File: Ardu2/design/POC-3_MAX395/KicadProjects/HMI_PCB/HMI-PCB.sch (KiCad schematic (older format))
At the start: 37 parts, among them P1 SplitPot_0_M, P10 TREM_VIB, P11 SplitPot_5_TR, P12 Analog Power IN, P13 Digital Power IN/OUT, P2 SEQ_SAVE, P3 SplitPot_1_A, P4 SplitPot_2_B, P5 PB_OUT, P6 Analog_Out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

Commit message: updated peripherals PCB
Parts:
- C1, C2, C3, C4, C5, C6: footprint Capacitors_ThroughHole:C_Radial_D5_L11_P2 -> misc:C_Radial_D5_L11_P3.81
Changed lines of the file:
@@
 F 0 "C1" H 1877 6935 50  0000 L CNN
 F 1 "1µF" H 1877 6846 50  0000 L CNN
-F 2 "Capacitors_ThroughHole:C_Radial_D5_L11_P2" H 1798 6740 50  0001 C CNN
+F 2 "misc:C_Radial_D5_L11_P3.81" H 1798 6740 50  0001 C CNN
 F 3 "" H 1760 6890 50  0000 C CNN
 	1    1760 6890
@@
 F 0 "C2" H 2527 6935 50  0000 L CNN
 F 1 "1µF" H 2527 6846 50  0000 L CNN
-F 2 "Capacitors_ThroughHole:C_Radial_D5_L11_P2" H 2448 6740 50  0001 C CNN
+F 2 "misc:C_Radial_D5_L11_P3.81" H 2448 6740 50  0001 C CNN
 F 3 "" H 2410 6890 50  0000 C CNN
 	1    2410 6890
@@
 F 0 "C5" H 4477 6935 50  0000 L CNN
 F 1 "1µF" H 4477 6846 50  0000 L CNN
-F 2 "Capacitors_ThroughHole:C_Radial_D5_L11_P2" H 4398 6740 50  0001 C CNN
+F 2 "misc:C_Radial_D5_L11_P3.81" H 4398 6740 50  0001 C CNN
 F 3 "" H 4360 6890 50  0000 C CNN
 	1    4360 6890
@@
 F 0 "C6" H 5127 6935 50  0000 L CNN
 F 1 "1µF" H 5127 6846 50  0000 L CNN
-F 2 "Capacitors_ThroughHole:C_Radial_D5_L11_P2" H 5048 6740 50  0001 C CNN
+F 2 "misc:C_Radial_D5_L11_P3.81" H 5048 6740 50  0001 C CNN
 F 3 "" H 5010 6890 50  0000 C CNN
 	1    5010 6890
@@
 F 0 "C3" H 3177 6935 50  0000 L CNN
 F 1 "1µF" H 3177 6846 50  0000 L CNN
-F 2 "Capacitors_ThroughHole:C_Radial_D5_L11_P2" H 3098 6740 50  0001 C CNN
+F 2 "misc:C_Radial_D5_L11_P3.81" H 3098 6740 50  0001 C CNN
 F 3 "" H 3060 6890 50  0000 C CNN
 	1    3060 6890
@@
 F 0 "C4" H 3827 6935 50  0000 L CNN
 F 1 "1µF" H 3827 6846 50  0000 L CNN
-F 2 "Capacitors_ThroughHole:C_Radial_D5_L11_P2" H 3748 6740 50  0001 C CNN
+F 2 "misc:C_Radial_D5_L11_P3.81" H 3748 6740 50  0001 C CNN
 F 3 "" H 3710 6890 50  0000 C CNN
 	1    3710 6890

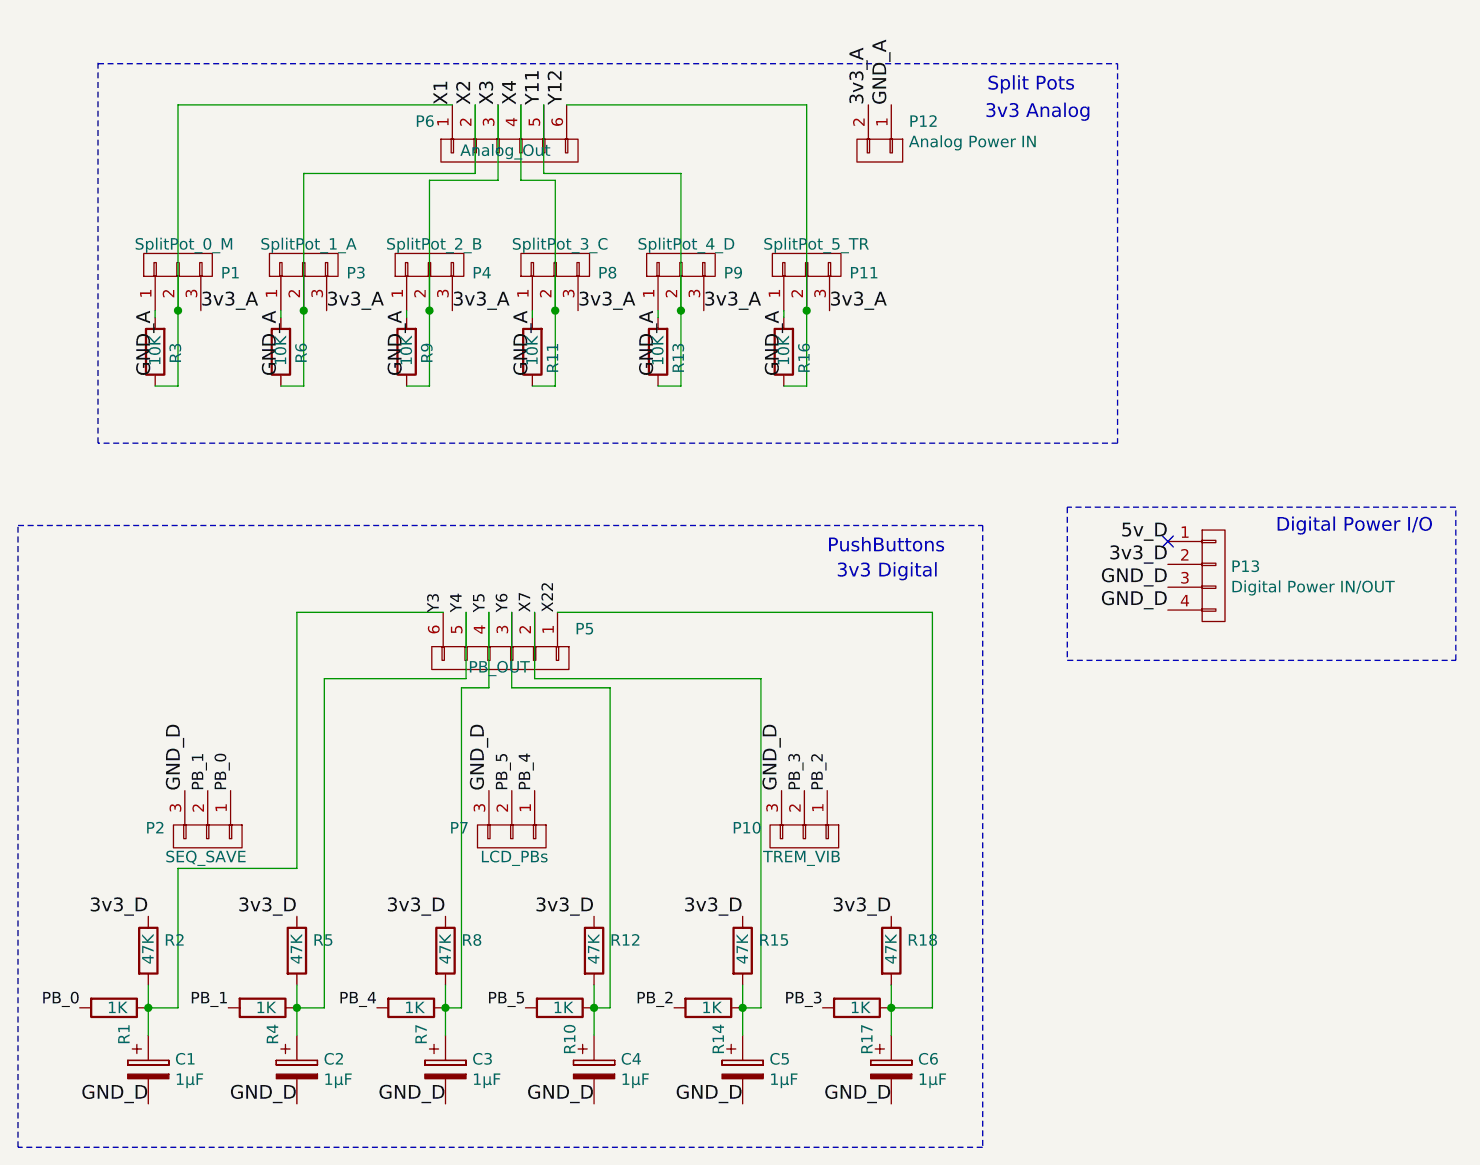
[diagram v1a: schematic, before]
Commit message: updated to HMI PCB after SENSEI review
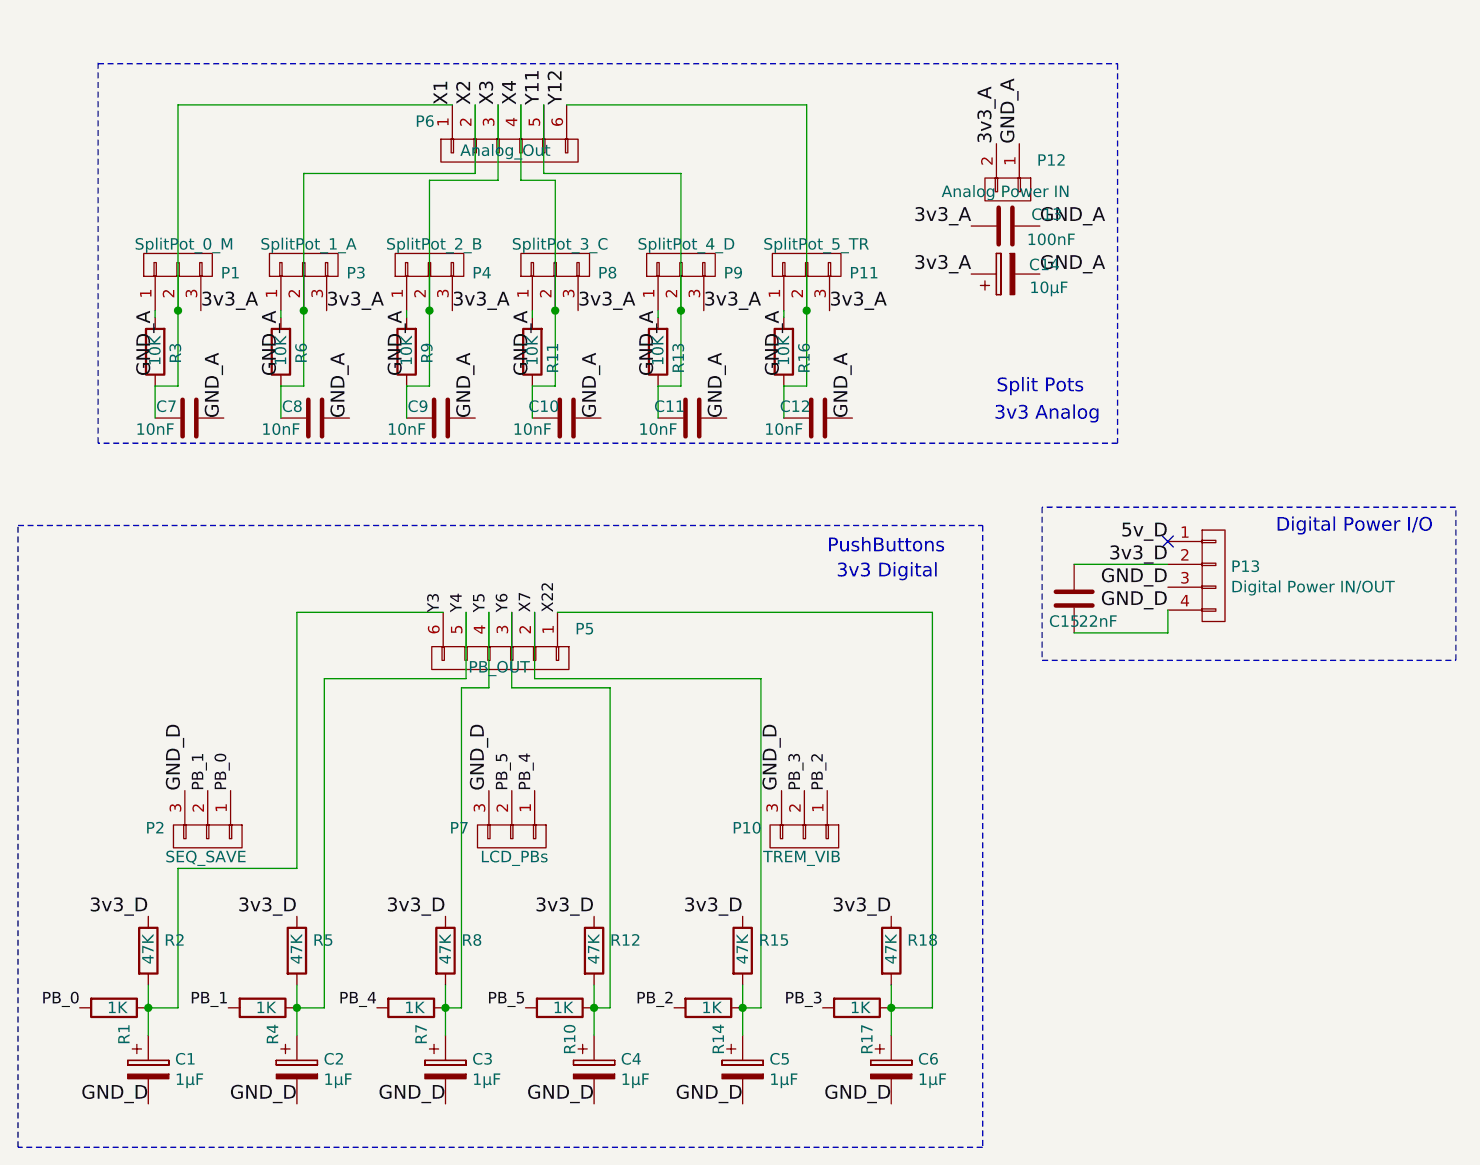
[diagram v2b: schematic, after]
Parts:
- added C10, C11, C12, C7, C8, C9: 10nF, Capacitors_ThroughHole:C_Disc_D6_P5, symbol C
- added C13: 100nF, Capacitors_ThroughHole:C_Disc_D3_P2.5, symbol C
- added C14: 10µF, Capacitors_ThroughHole:C_Radial_D5_L11_P2.5, symbol CP
- added C15: 22nF, Capacitors_ThroughHole:C_Rect_L7_W2.5_P5, symbol C
- P1, P10, P11, P2, P3, P4, P7, P8, P9: footprint Connect:Wafer_Horizontal10x5.8x7RM2.5-3 -> misc:Wafer_Angled_1x03_1mm_hole
- P12: footprint Pin_Headers:Pin_Header_Angled_1x02 -> misc:Wafer_Angled_1x02_1mm_hole
- P13: footprint Connect:bornier4 -> misc:bornier4_Dinkle
- P5, P6: footprint Connect:Wafer_Horizontal17.5x5.8x7RM2.5-6 -> misc:Wafer_Angled_1x06_1mm_Hole
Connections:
- net 3v3_A: now also C13.2, C14.1
- net 3v3_D: now also C15.1
- net GND_A: now also C10.1, C11.1, C12.1, C13.1, C14.2, C7.1, C8.1, C9.1
- net GND_D: now also C15.2
- net X1: now also C7.2
- net X2: now also C8.2
- net X3: now also C9.2
- net X4: now also C10.2
- net Y11: now also C11.2
- net Y12: now also C12.2
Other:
- moved on the sheet: P12
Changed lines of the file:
@@
 F 0 "P2" V 1984 5683 50  0000 R CNN
 F 1 "SEQ_SAVE" V 2110 6040 50  0000 R CNN
-F 2 "Connect:Wafer_Horizontal10x5.8x7RM2.5-3" H 2020 5870 50  0001 C CNN
+F 2 "misc:Wafer_Angled_1x03_1mm_hole" H 2020 5870 50  0001 C CNN
 F 3 "" H 2020 5870 50  0000 C CNN
 	1    2020 5870
@@
 F 0 "P1" V 1854 3183 50  0000 R CNN
 F 1 "SplitPot_0_M" V 1980 3560 50  0000 R CNN
-F 2 "Connect:Wafer_Horizontal10x5.8x7RM2.5-3" H 1890 3370 50  0001 C CNN
+F 2 "misc:Wafer_Angled_1x03_1mm_hole" H 1890 3370 50  0001 C CNN
 F 3 "" H 1890 3370 50  0000 C CNN
 	1    1890 3370
@@
 L CONN_01X02 P12
 U 1 1 580A7415
-P 4960 2870
-F 0 "P12" V 4833 2997 50  0000 L CNN
-F 1 "Analog Power IN" V 4922 2997 50  0000 L CNN
-F 2 "Pin_Headers:Pin_Header_Angled_1x02" H 4960 2870 50  0001 C CNN
-F 3 "" H 4960 2870 50  0000 C CNN
-	1    4960 2870
+P 5520 3040
+F 0 "P12" V 5393 3167 50  0000 L CNN
+F 1 "Analog Power IN" V 5530 2750 50  0000 L CNN
+F 2 "misc:Wafer_Angled_1x02_1mm_hole" H 5520 3040 50  0001 C CNN
+F 3 "" H 5520 3040 50  0000 C CNN
+	1    5520 3040
 	0    1    1    0
 $EndComp
@@
 F 0 "P6" V 3213 3197 50  0000 L CNN
 F 1 "Analog_Out" V 3340 2690 50  0000 L CNN
-F 2 "Connect:Wafer_Horizontal17.5x5.8x7RM2.5-6" H 3340 2870 50  0001 C CNN
+F 2 "misc:Wafer_Angled_1x06_1mm_Hole" H 3340 2870 50  0001 C CNN
 F 3 "" H 3340 2870 50  0000 C CNN
 	1    3340 2870
 	0    -1   1    0
 $EndComp
-Text Notes 5430 2620 0    60   ~ 0
+Text Notes 5470 3940 0    60   ~ 0
 Split Pots
 $Comp
@@
 F 0 "P5" V 3173 5417 50  0000 L CNN
 F 1 "PB_OUT" V 3340 4950 50  0000 L CNN
-F 2 "Connect:Wafer_Horizontal17.5x5.8x7RM2.5-6" H 3300 5090 50  0001 C CNN
+F 2 "misc:Wafer_Angled_1x06_1mm_Hole" H 3300 5090 50  0001 C CNN
 F 3 "" H 3300 5090 50  0000 C CNN
 	1    3300 5090
@@
 Text Notes 4770 4750 0    60   ~ 0
 3v3 Digital
-Text Notes 5420 2740 0    60   ~ 0
+Text Notes 5460 4060 0    60   ~ 0
 3v3 Analog
 $Comp
@@
 	1    0    0    -1
 $EndComp
-Text Label 4910 2670 1    60   ~ 0
+Text Label 5470 2840 1    60   ~ 0
 3v3_A
-Text Label 5010 2670 1    60   ~ 0
+Text Label 5570 2840 1    60   ~ 0
 GND_A
 Text Label 1790 3570 3    60   ~ 0
@@
 F 0 "P3" V 2404 3183 50  0000 R CNN
 F 1 "SplitPot_1_A" V 2530 3560 50  0000 R CNN
-F 2 "Connect:Wafer_Horizontal10x5.8x7RM2.5-3" H 2440 3370 50  0001 C CNN
+F 2 "misc:Wafer_Angled_1x03_1mm_hole" H 2440 3370 50  0001 C CNN
 F 3 "" H 2440 3370 50  0000 C CNN
 	1    2440 3370
@@
 F 0 "P4" V 2954 3183 50  0000 R CNN
 F 1 "SplitPot_2_B" V 3080 3560 50  0000 R CNN
-F 2 "Connect:Wafer_Horizontal10x5.8x7RM2.5-3" H 2990 3370 50  0001 C CNN
+F 2 "misc:Wafer_Angled_1x03_1mm_hole" H 2990 3370 50  0001 C CNN
 F 3 "" H 2990 3370 50  0000 C CNN
 	1    2990 3370
@@
 F 0 "P8" V 3504 3183 50  0000 R CNN
 F 1 "SplitPot_3_C" V 3630 3560 50  0000 R CNN
-F 2 "Connect:Wafer_Horizontal10x5.8x7RM2.5-3" H 3540 3370 50  0001 C CNN
+F 2 "misc:Wafer_Angled_1x03_1mm_hole" H 3540 3370 50  0001 C CNN
 F 3 "" H 3540 3370 50  0000 C CNN
 	1    3540 3370
@@
 F 0 "P9" V 4054 3183 50  0000 R CNN
 F 1 "SplitPot_4_D" V 4180 3560 50  0000 R CNN
-F 2 "Connect:Wafer_Horizontal10x5.8x7RM2.5-3" H 4090 3370 50  0001 C CNN
+F 2 "misc:Wafer_Angled_1x03_1mm_hole" H 4090 3370 50  0001 C CNN
 F 3 "" H 4090 3370 50  0000 C CNN
 	1    4090 3370
@@
 F 0 "P11" V 4604 3183 50  0000 R CNN
 F 1 "SplitPot_5_TR" V 4730 3560 50  0000 R CNN
-F 2 "Connect:Wafer_Horizontal10x5.8x7RM2.5-3" H 4640 3370 50  0001 C CNN
+F 2 "misc:Wafer_Angled_1x03_1mm_hole" H 4640 3370 50  0001 C CNN
 F 3 "" H 4640 3370 50  0000 C CNN
 	1    4640 3370
@@
 F 0 "P10" V 4594 5683 50  0000 R CNN
 F 1 "TREM_VIB" V 4720 6030 50  0000 R CNN
-F 2 "Connect:Wafer_Horizontal10x5.8x7RM2.5-3" H 4630 5870 50  0001 C CNN
+F 2 "misc:Wafer_Angled_1x03_1mm_hole" H 4630 5870 50  0001 C CNN
 F 3 "" H 4630 5870 50  0000 C CNN
 	1    4630 5870
@@
 F 0 "P7" V 3314 5683 50  0000 R CNN
 F 1 "LCD_PBs" V 3440 6030 50  0000 R CNN
-F 2 "Connect:Wafer_Horizontal10x5.8x7RM2.5-3" H 3350 5870 50  0001 C CNN
+F 2 "misc:Wafer_Angled_1x03_1mm_hole" H 3350 5870 50  0001 C CNN
 F 3 "" H 3350 5870 50  0000 C CNN
 	1    3350 5870
@@
 F 0 "P13" H 6496 4770 50  0000 L CNN
 F 1 "Digital Power IN/OUT" H 6496 4681 50  0000 L CNN
-F 2 "Connect:bornier4" H 6420 4730 50  0001 C CNN
+F 2 "misc:bornier4_Dinkle" H 6420 4730 50  0001 C CNN
 F 3 "" H 6420 4730 50  0000 C CNN
 	1    6420 4730
@@
 GND_D
 Wire Notes Line
-	5780 4430 5780 5100
-Wire Notes Line
-	5780 5100 7480 5100
+	5670 4430 5670 5100
+Wire Notes Line
+	5670 5100 7480 5100
 Wire Notes Line
 	7480 5100 7480 4430
 Wire Notes Line
-	7480 4430 5780 4430
+	7480 4430 5670 4430
 Text Notes 7380 4550 2    60   ~ 0
 Digital Power I/O
@@
 Connection ~ 4090 3570
 Connection ~ 4640 3570
+$Comp
+L C C13
+U 1 1 581098BB
+P 5510 3200
+F 0 "C13" V 5460 3380 50  0000 C CNN
+F 1 "100nF" V 5570 3400 50  0000 C CNN
+F 2 "Capacitors_ThroughHole:C_Disc_D3_P2.5" H 5548 3050 50  0001 C CNN
+F 3 "" H 5510 3200 50  0000 C CNN
+	1    5510 3200
+	0    1    1    0
+$EndComp
+$Comp
+L CP C14
+U 1 1 58109AF8
+P 5510 3410
+F 0 "C14" V 5550 3240 50  0000 C CNN
+F 1 "10µF" V 5450 3220 50  0000 C CNN
+F 2 "Capacitors_ThroughHole:C_Radial_D5_L11_P2.5" H 5548 3260 50  0001 C CNN
+F 3 "" H 5510 3410 50  0000 C CNN
+	1    5510 3410
+	0    -1   -1   0
+$EndComp
+Text Label 5360 3200 2    60   ~ 0
+3v3_A
+Text Label 5360 3410 2    60   ~ 0
+3v3_A
+Text Label 5660 3200 0    60   ~ 0
+GND_A
+Text Label 5660 3410 0    60   ~ 0
+GND_A
+$Comp
+L C C7
+U 1 1 5810ACDC
+P 1940 4040
+F 0 "C7" V 1890 3940 50  0000 C CNN
+F 1 "10nF" V 1990 3890 50  0000 C CNN
+F 2 "Capacitors_ThroughHole:C_Disc_D6_P5" H 1978 3890 50  0001 C CNN
+F 3 "" H 1940 4040 50  0000 C CNN
+	1    1940 4040
+	0    1    1    0
+$EndComp
+Wire Wire Line
+	1790 3900 1790 4040
+Text Label 2090 4040 1    60   ~ 0
+GND_A
+$Comp
+L C C8
+U 1 1 5810B6B9
+P 2490 4040
+F 0 "C8" V 2440 3940 50  0000 C CNN
+F 1 "10nF" V 2540 3890 50  0000 C CNN
+F 2 "Capacitors_ThroughHole:C_Disc_D6_P5" H 2528 3890 50  0001 C CNN
+F 3 "" H 2490 4040 50  0000 C CNN
+	1    2490 4040
+	0    1    1    0
+$EndComp
+Wire Wire Line
+	2340 3900 2340 4040
+Text Label 2640 4040 1    60   ~ 0
+GND_A
+$Comp
+L C C9
+U 1 1 5810B83D
+P 3040 4040
+F 0 "C9" V 2990 3940 50  0000 C CNN
+F 1 "10nF" V 3090 3890 50  0000 C CNN
+F 2 "Capacitors_ThroughHole:C_Disc_D6_P5" H 3078 3890 50  0001 C CNN
+F 3 "" H 3040 4040 50  0000 C CNN
+	1    3040 4040
+	0    1    1    0
+$EndComp
+Wire Wire Line
+	2890 3900 2890 4040
+Text Label 3190 4040 1    60   ~ 0
+GND_A
+$Comp
+L C C10
+U 1 1 5810B845
+P 3590 4040
+F 0 "C10" V 3540 3940 50  0000 C CNN
+F 1 "10nF" V 3640 3890 50  0000 C CNN
+F 2 "Capacitors_ThroughHole:C_Disc_D6_P5" H 3628 3890 50  0001 C CNN
+F 3 "" H 3590 4040 50  0000 C CNN
+	1    3590 4040
+	0    1    1    0
+$EndComp
+Wire Wire Line
+	3440 3900 3440 4040
+Text Label 3740 4040 1    60   ~ 0
+GND_A
+$Comp
+L C C11
+U 1 1 5810BB2B
+P 4140 4040
+F 0 "C11" V 4090 3940 50  0000 C CNN
+F 1 "10nF" V 4190 3890 50  0000 C CNN
+F 2 "Capacitors_ThroughHole:C_Disc_D6_P5" H 4178 3890 50  0001 C CNN
+F 3 "" H 4140 4040 50  0000 C CNN
+	1    4140 4040
+	0    1    1    0
+$EndComp
+Wire Wire Line
+	3990 3900 3990 4040
+Text Label 4290 4040 1    60   ~ 0
+GND_A
+$Comp
+L C C12
+U 1 1 5810BB33
+P 4690 4040
+F 0 "C12" V 4640 3940 50  0000 C CNN
+F 1 "10nF" V 4740 3890 50  0000 C CNN
+F 2 "Capacitors_ThroughHole:C_Disc_D6_P5" H 4728 3890 50  0001 C CNN
+F 3 "" H 4690 4040 50  0000 C CNN
+	1    4690 4040
+	0    1    1    0
+$EndComp
+Wire Wire Line
+	4540 3900 4540 4040
+Text Label 4840 4040 1    60   ~ 0
+GND_A
+$Comp
+L C C15
+U 1 1 5810BF8D
+P 5810 4830
+F 0 "C15" H 5700 4730 50  0000 L CNN
+F 1 "22nF" H 5830 4730 50  0000 L CNN
+F 2 "Capacitors_ThroughHole:C_Rect_L7_W2.5_P5" H 5848 4680 50  0001 C CNN
+F 3 "" H 5810 4830 50  0000 C CNN
+	1    5810 4830
+	1    0    0    -1
+$EndComp
+Wire Wire Line
+	6220 4680 5810 4680
+Wire Wire Line
+	5810 4980 6220 4980
+Wire Wire Line
+	6220 4980 6220 4880
 $EndSCHEMATC

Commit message: updated to HMI PCB after second SENSEI review
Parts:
- added C16: 1µF, Capacitors_ThroughHole:C_Radial_D5_L6_P2.5, symbol C
- added L1: 10mH, Resistors_ThroughHole:Resistor_Horizontal_RM10mm, symbol INDUCTOR_Small
- P6: value Analog_Out -> Analog_Signal_Out
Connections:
- net 3v3_A: now also C16.1, L1.1; no longer P12.2 (P2)
- net GND_A: now also C16.2
- new net 3v3_A_IN: L1.2, P12.2 (P2)
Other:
- moved on the sheet: C13, C14, P12
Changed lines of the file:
@@
 encoding utf-8
 Sheet 1 1
-Title ""
-Date ""
-Rev ""
-Comp ""
-Comment1 ""
+Title "PyGuitar Peripherals &
+"
+Date "2016-10-28"
+Rev "1.3"
+Comp "PyGuitar.org"
+Comment1 "Added LC filter to analog power input"
 Comment2 ""
 Comment3 ""
@@
 L CONN_01X02 P12
 U 1 1 580A7415
-P 5520 3040
-F 0 "P12" V 5393 3167 50  0000 L CNN
-F 1 "Analog Power IN" V 5530 2750 50  0000 L CNN
-F 2 "misc:Wafer_Angled_1x02_1mm_hole" H 5520 3040 50  0001 C CNN
-F 3 "" H 5520 3040 50  0000 C CNN
-	1    5520 3040
+P 5910 3040
+F 0 "P12" V 5783 3167 50  0000 L CNN
+F 1 "Analog Power IN" V 5480 2260 50  0000 L CNN
+F 2 "misc:Wafer_Angled_1x02_1mm_hole" H 5910 3040 50  0001 C CNN
+F 3 "" H 5910 3040 50  0000 C CNN
+	1    5910 3040
 	0    1    1    0
 $EndComp
@@
 P 3340 2870
 F 0 "P6" V 3213 3197 50  0000 L CNN
-F 1 "Analog_Out" V 3340 2690 50  0000 L CNN
+F 1 "Analog_Signal_Out" V 3340 2530 50  0000 L CNN
 F 2 "misc:Wafer_Angled_1x06_1mm_Hole" H 3340 2870 50  0001 C CNN
 F 3 "" H 3340 2870 50  0000 C CNN
@@
 	0    -1   1    0
 $EndComp
-Text Notes 5470 3940 0    60   ~ 0
+Text Notes 6010 3960 0    60   ~ 0
 Split Pots
 $Comp
@@
 Text Notes 4770 4750 0    60   ~ 0
 3v3 Digital
-Text Notes 5460 4060 0    60   ~ 0
+Text Notes 6000 4080 0    60   ~ 0
 3v3 Analog
 $Comp
@@
 	1    0    0    -1
 $EndComp
-Text Label 5470 2840 1    60   ~ 0
+Text Label 5750 3410 2    60   ~ 0
 3v3_A
-Text Label 5570 2840 1    60   ~ 0
+Text Label 5960 2840 1    60   ~ 0
 GND_A
 Text Label 1790 3570 3    60   ~ 0
@@
 Y6
 Wire Notes Line
-	6000 4150 1540 4150
-Wire Notes Line
-	1540 4150 1540 2480
-Wire Notes Line
-	1540 2490 6000 2490
-Wire Notes Line
-	6000 2490 6000 4150
+	1540 4150 6580 4150
+Wire Notes Line
+	1540 2290 1540 4150
 Wire Wire Line
 	1890 2670 1890 3900
@@
 L C C13
 U 1 1 581098BB
-P 5510 3200
-F 0 "C13" V 5460 3380 50  0000 C CNN
-F 1 "100nF" V 5570 3400 50  0000 C CNN
-F 2 "Capacitors_ThroughHole:C_Disc_D3_P2.5" H 5548 3050 50  0001 C CNN
-F 3 "" H 5510 3200 50  0000 C CNN
-	1    5510 3200
+P 5900 3200
+F 0 "C13" V 5860 3080 50  0000 C CNN
+F 1 "100nF" V 5960 3400 50  0000 C CNN
+F 2 "Capacitors_ThroughHole:C_Disc_D3_P2.5" H 5938 3050 50  0001 C CNN
+F 3 "" H 5900 3200 50  0000 C CNN
+	1    5900 3200
 	0    1    1    0
 $EndComp
@@
 L CP C14
 U 1 1 58109AF8
-P 5510 3410
-F 0 "C14" V 5550 3240 50  0000 C CNN
-F 1 "10µF" V 5450 3220 50  0000 C CNN
-F 2 "Capacitors_ThroughHole:C_Radial_D5_L11_P2.5" H 5548 3260 50  0001 C CNN
-F 3 "" H 5510 3410 50  0000 C CNN
-	1    5510 3410
+P 5900 3410
+F 0 "C14" V 5980 3510 50  0000 C CNN
+F 1 "10µF" V 5840 3220 50  0000 C CNN
+F 2 "Capacitors_ThroughHole:C_Radial_D5_L11_P2.5" H 5938 3260 50  0001 C CNN
+F 3 "" H 5900 3410 50  0000 C CNN
+	1    5900 3410
 	0    -1   -1   0
 $EndComp
-Text Label 5360 3200 2    60   ~ 0
-3v3_A
-Text Label 5360 3410 2    60   ~ 0
-3v3_A
-Text Label 5660 3200 0    60   ~ 0
-GND_A
-Text Label 5660 3410 0    60   ~ 0
-GND_A
 $Comp
 L C C7
@@
 U 1 1 5810BF8D
 P 5810 4830
-F 0 "C15" H 5700 4730 50  0000 L CNN
+F 0 "C15" H 5750 4910 50  0000 L CNN
 F 1 "22nF" H 5830 4730 50  0000 L CNN
 F 2 "Capacitors_ThroughHole:C_Rect_L7_W2.5_P5" H 5848 4680 50  0001 C CNN
@@
 Wire Wire Line
 	6220 4980 6220 4880
+$Comp
+L INDUCTOR_Small L1
+U 1 1 5813167B
+P 5590 3630
+F 0 "L1" V 5550 3640 50  0000 C CNN
+F 1 "10mH" V 5670 3620 50  0000 C CNN
+F 2 "Resistors_ThroughHole:Resistor_Horizontal_RM10mm" H 5590 3630 50  0001 C CNN
+F 3 "" H 5590 3630 50  0000 C CNN
+	1    5590 3630
+	0    1    1    0
+$EndComp
+Wire Notes Line
+	6580 4150 6580 2490
+Wire Wire Line
+	5750 3200 5750 3630
+Connection ~ 5750 3410
+$Comp
+L C C16
+U 1 1 581341E9
+P 5900 3630
+F 0 "C16" V 5850 3540 50  0000 C CNN
+F 1 "1µF" V 5950 3780 50  0000 C CNN
+F 2 "Capacitors_ThroughHole:C_Radial_D5_L6_P2.5" H 5938 3480 50  0001 C CNN
+F 3 "" H 5900 3630 50  0000 C CNN
+	1    5900 3630
+	0    -1   -1   0
+$EndComp
+Wire Wire Line
+	5750 3630 5690 3630
+Text Label 5860 2840 1    60   ~ 0
+3v3_A_IN
+Wire Wire Line
+	6050 2840 6050 3630
+Connection ~ 6050 3410
+Wire Wire Line
+	5960 2840 6050 2840
+Connection ~ 6050 3200
+Wire Wire Line
+	5490 3630 5490 2840
+Wire Wire Line
+	5490 2840 5860 2840
+Wire Notes Line
+	6580 2500 6580 2290
+Wire Notes Line
+	6580 2290 1540 2290
 $EndSCHEMATC
